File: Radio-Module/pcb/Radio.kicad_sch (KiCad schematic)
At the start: 0 parts

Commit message: Worked on Radio Transciever
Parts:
- added C10, C11, C12, C13, C4, C5, C7, C8, C9: 47nF, Capacitor_SMD:C_0603_1608Metric, symbol Device:C
- added C14: 10nF, Capacitor_SMD:C_0603_1608Metric, symbol Device:C
- added C15, C16: 10pF, Capacitor_SMD:C_0603_1608Metric, symbol Device:C
- added C17, C18, C19: 5.1pF, Capacitor_SMD:C_0603_1608Metric, symbol Device:C
- added C20: 2.2pF, Capacitor_SMD:C_0603_1608Metric, symbol Device:C
- added C3: 1.8nF, Capacitor_SMD:C_0603_1608Metric, symbol Device:C
- added C6: 0.22uF, Capacitor_SMD:C_0603_1608Metric, symbol Device:C
- added L1: 56nH, Inductor_SMD:L_0603_1608Metric, symbol Device:L
- added L2, L4: 27nH, Inductor_SMD:L_0603_1608Metric, symbol Device:L
- added L3, L5: 15nH, Inductor_SMD:L_0603_1608Metric, symbol Device:L
- added R1: 56k, Resistor_SMD:R_0603_1608Metric, symbol Device:R_US
- added U2: CC1200, Package_DFN_QFN:QFN-32-1EP_5x5mm_P0.5mm_EP3.45x3.45mm, symbol RF:CC1200
- added Y1: Crystal_GND2, symbol Device:Crystal_GND2
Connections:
- new net: C20.1, L5.1
- new net: C19.1, C20.2, L5.2
- new net: C14.2, U2.21 (DCPL_VCO)
- new net: C10.1, U2.26 (DCPL_PFD_CHP)
- new net: C12.1, U2.29 (DCPL_XOSC)
- new net: R1.1, U2.14 (RBIAS)
- new net: C18.1, L1.2, L4.1
- new net: C15.1, U2.31 (XOSC_Q2), Y1.1
- new net: C16.1, U2.30 (XOSC_Q1), Y1.3
- new net: C3.1, U2.23 (LPF0)
- new net: C3.2, U2.24 (LPF1)
- new net: C18.2, L2.2, L3.1
- new net: C6.1, U2.6 (DCPL)
- new net: C19.2, L3.2
- new net: C17.1, L1.1, L2.1
- new net +3.3V: C11.1, C13.2, C4.1, C5.1, C7.1, C8.1, C9.1, U2.1 (VDD_GUARD), U2.12 (DVDD), U2.13 (AVDD_IF), U2.15 (AVDD_RF), U2.22 (AVDD_SYNTH1), U2.25 (AVDD_PFD_CHP), U2.27 (AVDD_SYNTH2), U2.28 (AVDD_XOSC), U2.5 (DVDD)
- new net GND: C10.2, C11.2, C12.2, C13.1, C14.1, C15.2, C16.2, C17.2, C4.2, C5.2, C6.2, C7.2, C8.2, C9.2, L4.2, R1.2, U2.32 (EXT_XOSC), U2.33 (GND_EP), Y1.2
- new net SCLK_Radio: U2.8 (SCLK)
- new net miso_Radio: U2.9 (SO(GPIO1))
- new net mosi_Radio: U2.7 (SI)
- new net reset_Radio: U2.2 (~{RESET})
- no-connect marks 0 -> 1

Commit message: Finished radio module
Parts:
- added C21: 39pF, Capacitor_SMD:C_0603_1608Metric, symbol Device:C
- added C22: 56pF, Capacitor_SMD:C_0603_1608Metric, symbol Device:C
- added C23: 100pF, Capacitor_SMD:C_0603_1608Metric, symbol Device:C
- added C24: 6.2pF, Capacitor_SMD:C_0603_1608Metric, symbol Device:C
- added C25: 10nF, Capacitor_SMD:C_0603_1608Metric, symbol Device:C
- added L6: 43nH, Inductor_SMD:L_0603_1608Metric, symbol Device:L
- added L7: 22nH, Inductor_SMD:L_0603_1608Metric, symbol Device:L
- added L8: 56nH, Inductor_SMD:L_0603_1608Metric, symbol Device:L
- added R1: 18, Resistor_SMD:R_0603_1608Metric_Pad0.98x0.95mm_HandSolder, symbol Device:R_US
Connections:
- net +3.3V: now also C22.2, C23.1, C25.1, R1.2
- net GND: now also C23.2, C24.1, C25.2
- net at C20.1, L5.1: now also C21.2
- net at C19.1, C20.2, L5.2: now also L6.1
- net at C18.1, L1.2, L4.1: now also U2.19 (LNA_P)
- net at C19.2, L3.2: now also U2.18 (TRX_SW)
- net at C17.1, L1.1, L2.1: now also U2.20 (LNA_N)
- net CS_radio: now reaches U2.11 (~{CS})
- net at U2.17 (PA): now also C21.1, L8.1
- net radio_marc_int_GPIO3: now reaches U2.3 (GPIO3)
- net radio_int_GPIO2: now reaches U2.4 (GPIO2)
- new net: C22.1, L8.2, R1.1
- new net: C24.2, L6.2, L7.1
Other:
- moved on the sheet: C19, C20, L1, L3, L4, L5

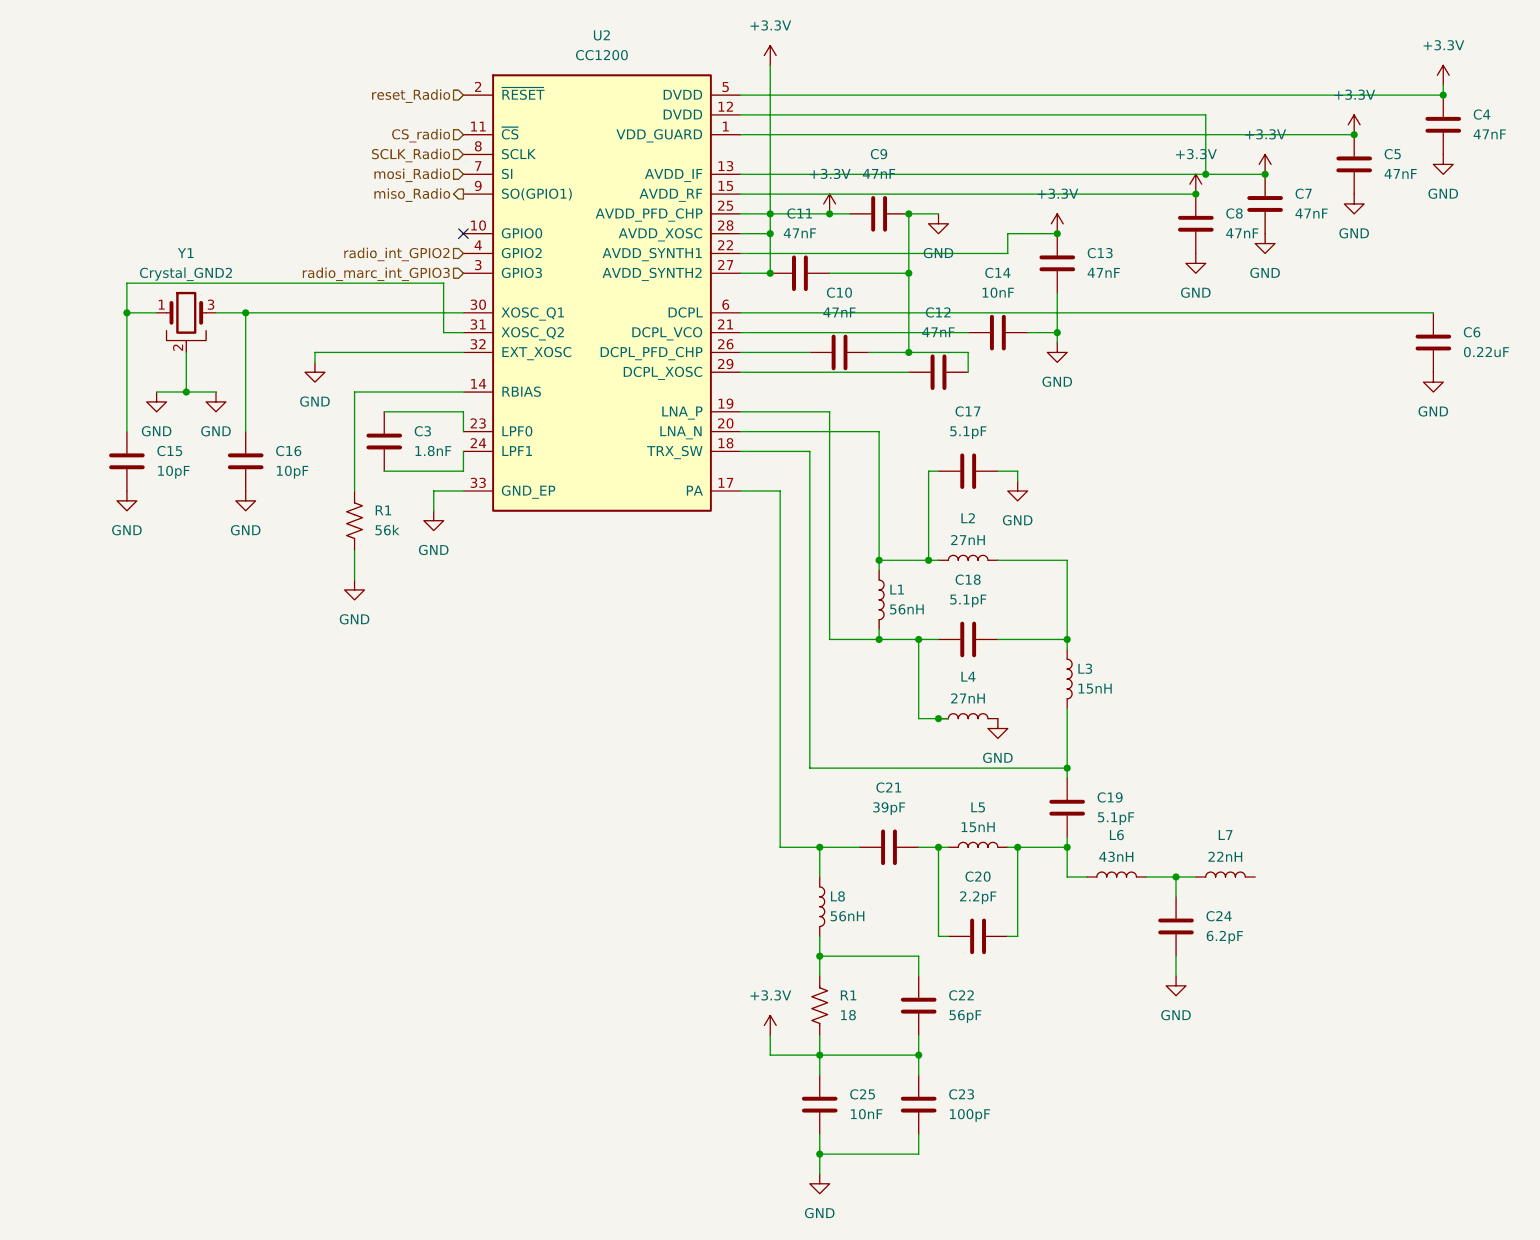
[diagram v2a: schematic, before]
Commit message: Fixed Oscillator and SMA Connector for radio module
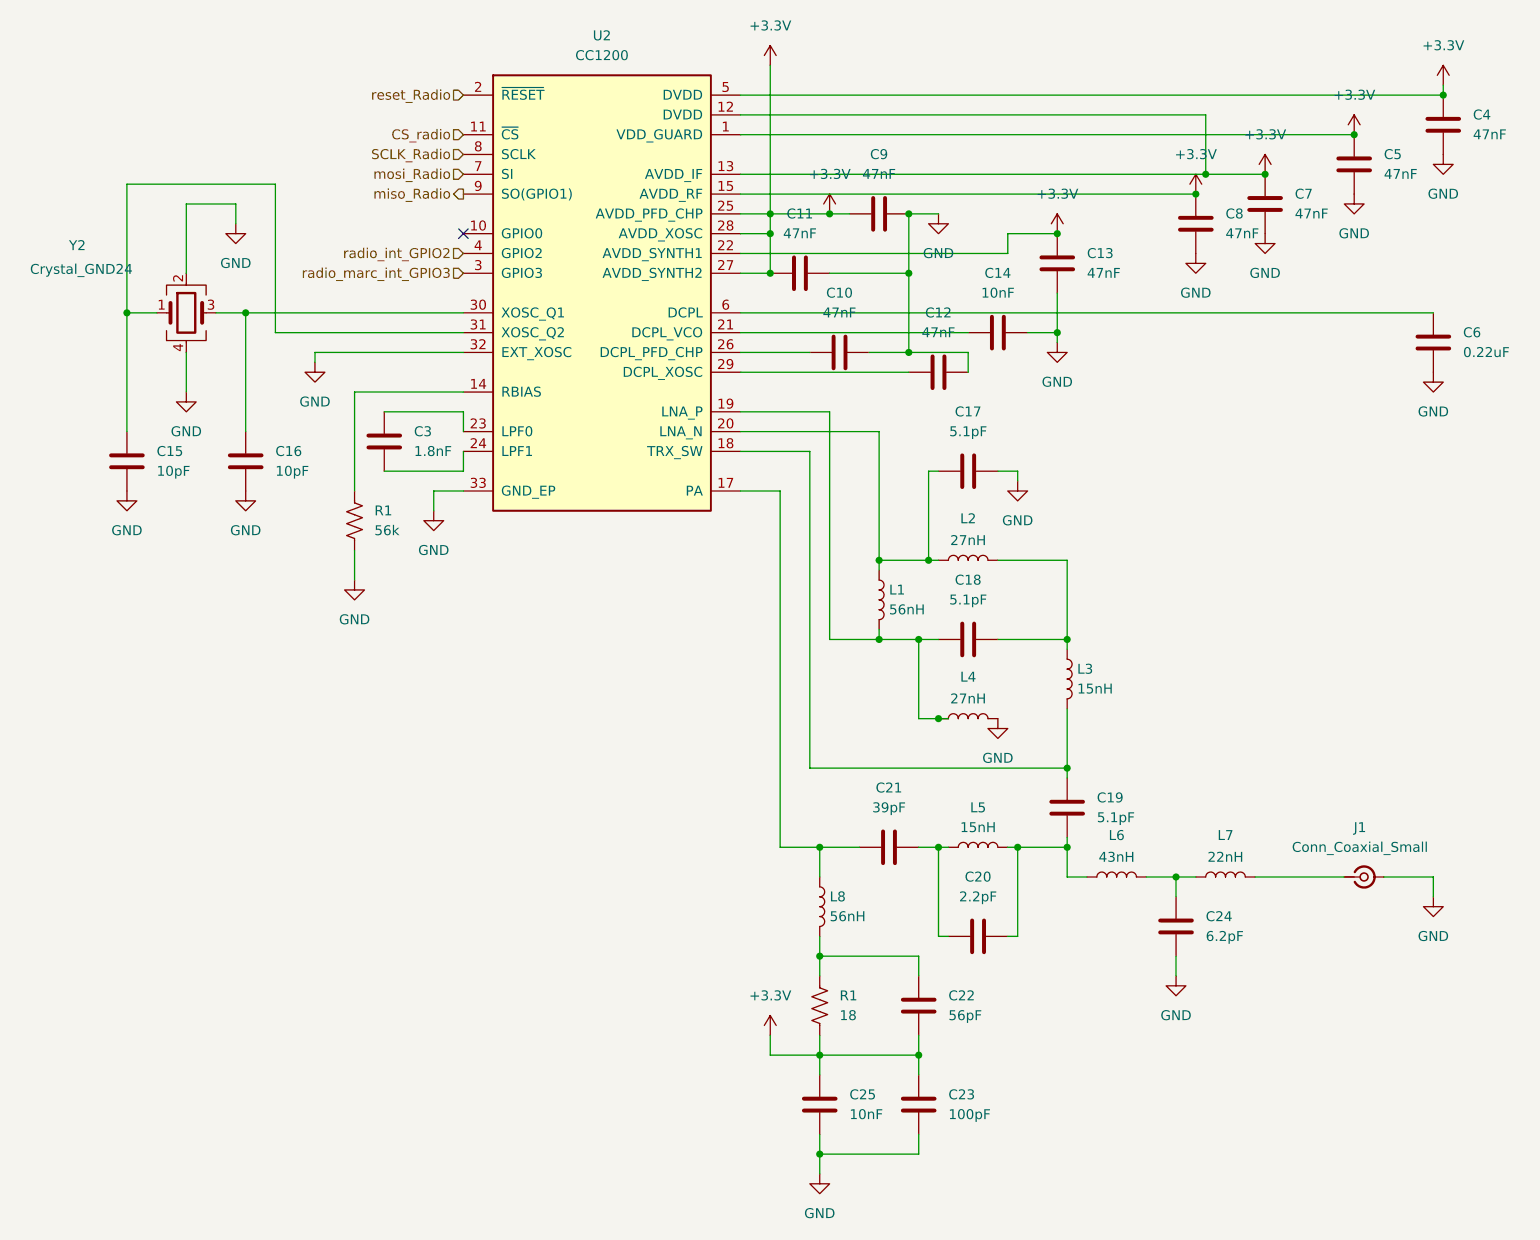
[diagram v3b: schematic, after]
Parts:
- removed Y1: Crystal_GND2, symbol Device:Crystal_GND2
- added J1: Conn_Coaxial_Small, symbol Connector:Conn_Coaxial_Small
- added Y2: Crystal_GND24, symbol Device:Crystal_GND24
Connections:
- net GND: now also J1.2 (Ext), Y2.2, Y2.4
- net at C15.1, U2.31 (XOSC_Q2): now also Y2.1
- net at C16.1, U2.30 (XOSC_Q1): now also Y2.3
- net at L7.2: now also J1.1 (In)
